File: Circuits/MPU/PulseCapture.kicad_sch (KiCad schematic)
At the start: 24 parts, among them U26 LT1715, U27 ADA4805-2ARMZ, U31 AD7984BRMZ

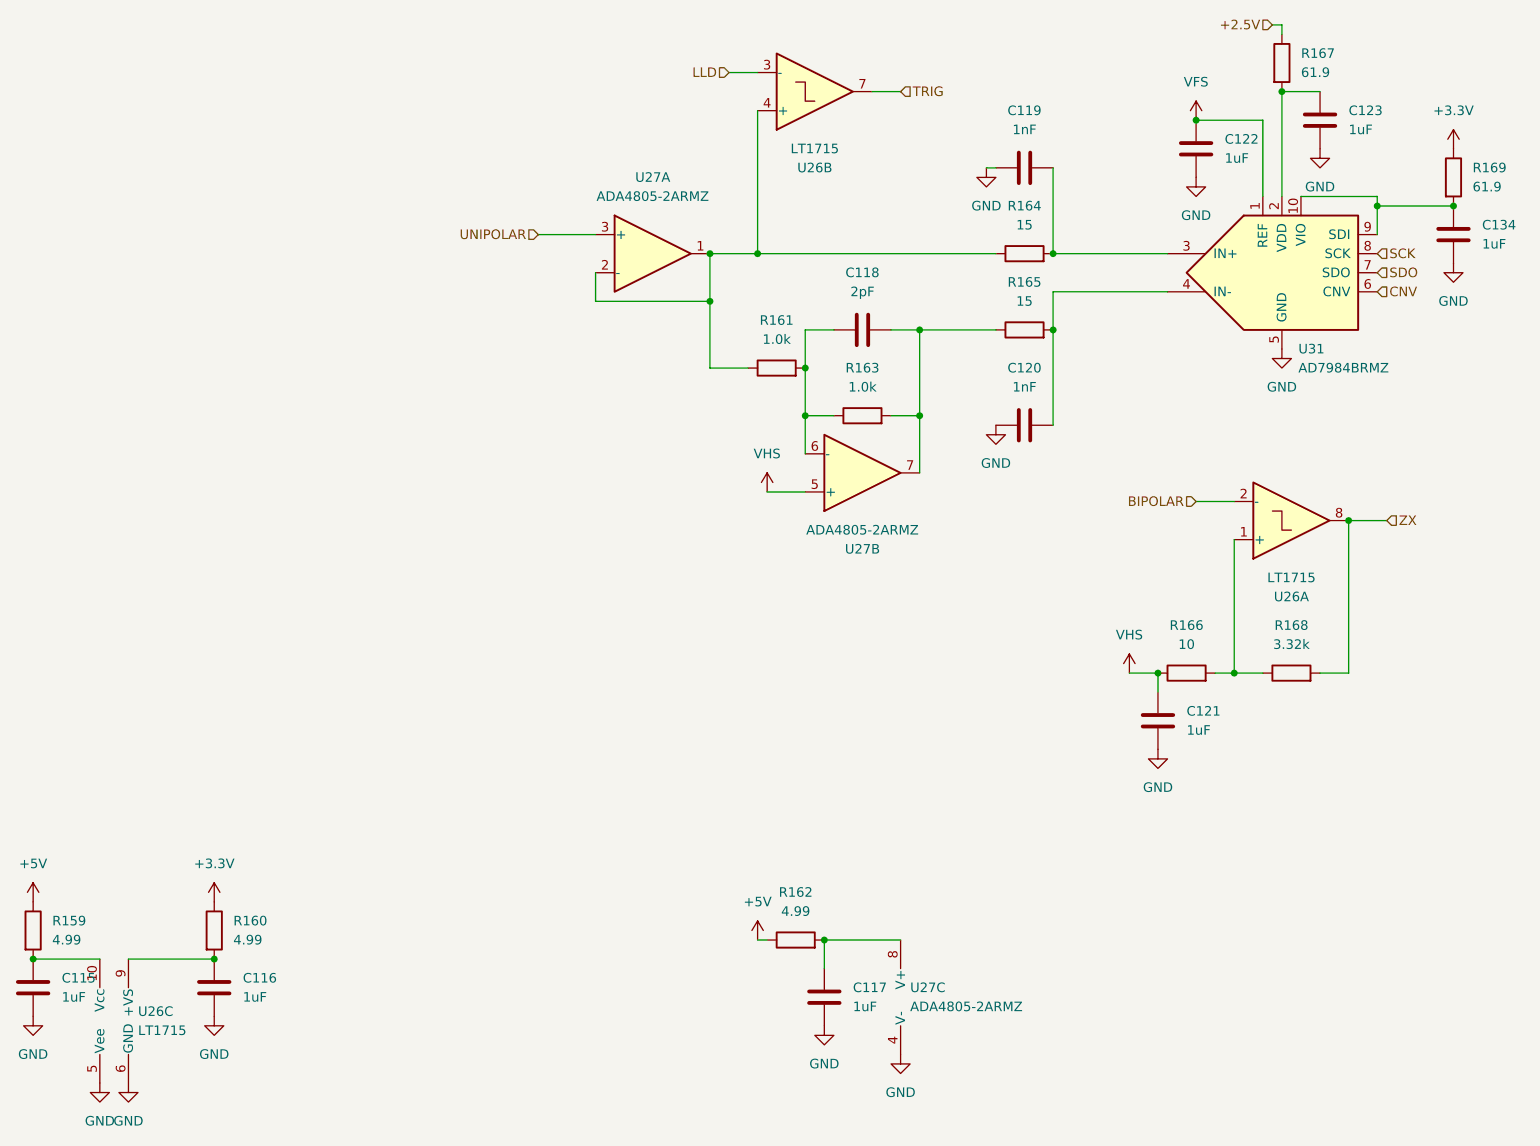
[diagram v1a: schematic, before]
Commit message: PPS is RS422, add MXINH
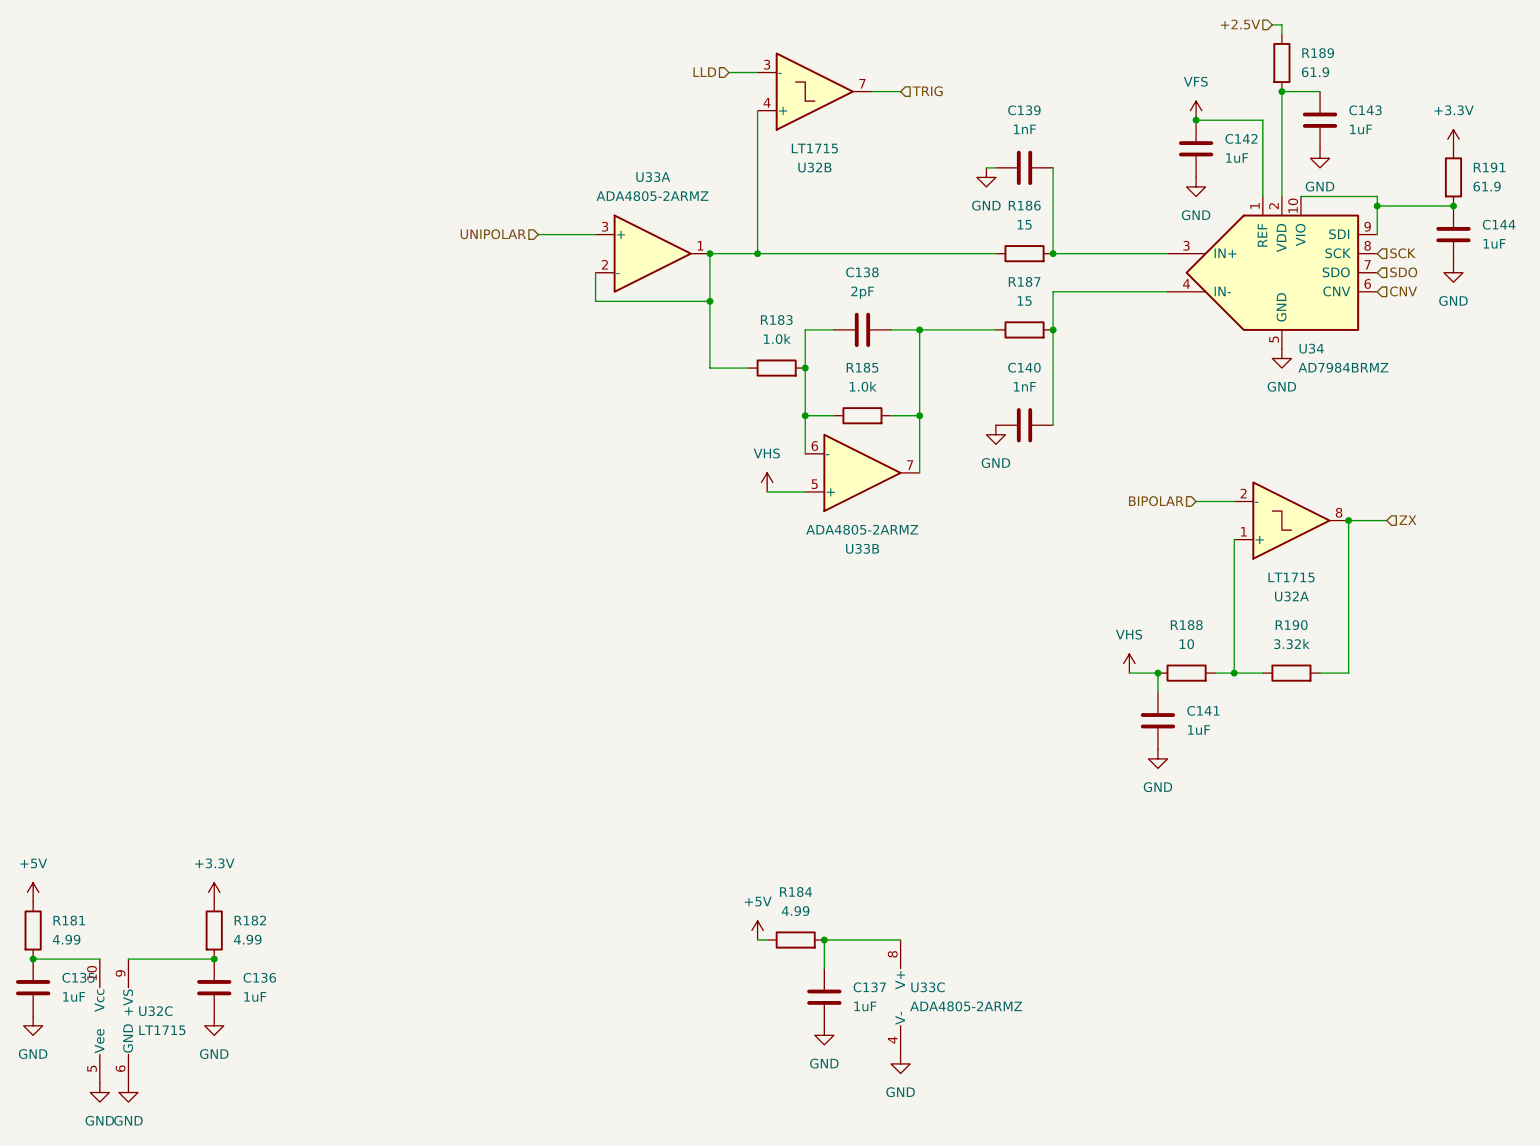
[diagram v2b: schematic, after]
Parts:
- renumbered C115 to C135, C116 to C136, C117 to C137, C118 to C138, C119 to C139, C120 to C140, C121 to C141, C122 to C142, C123 to C143, C134 to C144, R159 to R181, R160 to R182, R161 to R183, R162 to R184, R163 to R185, R164 to R186, R165 to R187, R166 to R188, R167 to R189, R168 to R190, R169 to R191, U26 to U32, U27 to U33, U31 to U34
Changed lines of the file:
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@@
 	(title_block
 		(title "QuERI MPU")
-		(date "2024-06-05")
-		(rev "RR1")
+		(date "2024-06-27")
+		(rev "RR3")
 		(company "Noqsi Aerospace Ltd")
 		(comment 1 "15 Blanchard Avenue, Billerica MA 01821")
@@
 		(dnp no)
 		(fields_autoplaced yes)
-		(property "Reference" "#PWR0230"
+		(property "Reference" "#PWR0270"
 			(at 31.75 201.93 0)
 			(effects
@@
 		(dnp no)
 		(fields_autoplaced yes)
-		(property "Reference" "C123"
+		(property "Reference" "C143"
 			(at 198.12 66.04 0)
 			(effects
@@
 		(dnp no)
 		(fields_autoplaced yes)
-		(property "Reference" "C120"
+		(property "Reference" "C140"
 			(at 154.94 100.33 90)
 			(effects
@@
 		(on_board yes)
 		(dnp no)
-		(property "Reference" "U27"
+		(property "Reference" "U33"
 			(at 133.35 124.46 0)
 			(effects
@@
 		(dnp no)
 		(fields_autoplaced yes)
-		(property "Reference" "C117"
+		(property "Reference" "C137"
 			(at 132.08 182.88 0)
 			(effects
@@
 		(dnp no)
 		(fields_autoplaced yes)
-		(property "Reference" "C134"
+		(property "Reference" "C144"
 			(at 215.9 81.28 0)
 			(effects
@@
 		(dnp no)
 		(fields_autoplaced yes)
-		(property "Reference" "R165"
+		(property "Reference" "R187"
 			(at 154.94 88.9 90)
 			(effects
@@
 		(dnp no)
 		(fields_autoplaced yes)
-		(property "Reference" "#PWR0241"
+		(property "Reference" "#PWR0281"
 			(at 172.72 157.48 0)
 			(effects
@@
 		(dnp no)
 		(fields_autoplaced yes)
-		(property "Reference" "#PWR0229"
+		(property "Reference" "#PWR0269"
 			(at 22.86 193.04 0)
 			(effects
@@
 		(dnp no)
 		(fields_autoplaced yes)
-		(property "Reference" "U27"
+		(property "Reference" "U33"
 			(at 139.7 182.88 0)
 			(effects
@@
 		(dnp no)
 		(fields_autoplaced yes)
-		(property "Reference" "C118"
+		(property "Reference" "C138"
 			(at 133.35 87.63 90)
 			(effects
@@
 		(dnp no)
 		(fields_autoplaced yes)
-		(property "Reference" "#PWR0232"
+		(property "Reference" "#PWR0272"
 			(at 46.99 175.26 0)
 			(effects
@@
 		(dnp no)
 		(fields_autoplaced yes)
-		(property "Reference" "#PWR0267"
+		(property "Reference" "#PWR0287"
 			(at 212.09 92.71 0)
 			(effects
@@
 		(dnp no)
 		(fields_autoplaced yes)
-		(property "Reference" "U27"
+		(property "Reference" "U33"
 			(at 105.41 74.93 0)
 			(effects
@@
 		(dnp no)
 		(fields_autoplaced yes)
-		(property "Reference" "R162"
+		(property "Reference" "R184"
 			(at 124.46 170.18 90)
 			(effects
@@
 		(dnp no)
 		(fields_autoplaced yes)
-		(property "Reference" "#PWR0228"
+		(property "Reference" "#PWR0268"
 			(at 22.86 175.26 0)
 			(effects
@@
 		(dnp no)
 		(fields_autoplaced yes)
-		(property "Reference" "R164"
+		(property "Reference" "R186"
 			(at 154.94 78.74 90)
 			(effects
@@
 		(dnp no)
 		(fields_autoplaced yes)
-		(property "Reference" "#PWR0243"
+		(property "Reference" "#PWR0283"
 			(at 177.8 81.28 0)
 			(effects
@@
 		(dnp no)
 		(fields_autoplaced yes)
-		(property "Reference" "#PWR0239"
+		(property "Reference" "#PWR0279"
 			(at 151.13 114.3 0)
 			(effects
@@
 		(dnp no)
 		(fields_autoplaced yes)
-		(property "Reference" "#PWR0246"
+		(property "Reference" "#PWR0286"
 			(at 212.09 74.93 0)
 			(effects
@@
 		(dnp no)
 		(fields_autoplaced yes)
-		(property "Reference" "#PWR0238"
+		(property "Reference" "#PWR0278"
 			(at 149.86 80.01 0)
 			(effects
@@
 		(dnp no)
 		(fields_autoplaced yes)
-		(property "Reference" "R167"
+		(property "Reference" "R189"
 			(at 191.77 58.42 0)
 			(effects
@@
 		(dnp no)
 		(fields_autoplaced yes)
-		(property "Reference" "R166"
+		(property "Reference" "R188"
 			(at 176.53 134.62 90)
 			(effects
@@
 		(dnp no)
 		(fields_autoplaced yes)
-		(property "Reference" "#PWR0235"
+		(property "Reference" "#PWR0275"
 			(at 120.65 120.65 0)
 			(effects
@@
 		(dnp no)
 		(fields_autoplaced yes)
-		(property "Reference" "C116"
+		(property "Reference" "C136"
 			(at 50.8 181.61 0)
 			(effects
@@
 		(dnp no)
 		(fields_autoplaced yes)
-		(property "Reference" "C115"
+		(property "Reference" "C135"
 			(at 26.67 181.61 0)
 			(effects
@@
 		(on_board yes)
 		(dnp no)
-		(property "Reference" "U26"
+		(property "Reference" "U32"
 			(at 190.5 130.81 0)
 			(effects
@@
 		(dnp no)
 		(fields_autoplaced yes)
-		(property "Reference" "#PWR0236"
+		(property "Reference" "#PWR0276"
 			(at 128.27 194.31 0)
 			(effects
@@
 		(dnp no)
 		(fields_autoplaced yes)
-		(property "Reference" "C122"
+		(property "Reference" "C142"
 			(at 181.61 69.85 0)
 			(effects
@@
 		(dnp no)
 		(fields_autoplaced yes)
-		(property "Reference" "#PWR0245"
+		(property "Reference" "#PWR0285"
 			(at 194.31 77.47 0)
 			(effects
@@
 		(dnp no)
 		(fields_autoplaced yes)
-		(property "Reference" "C119"
+		(property "Reference" "C139"
 			(at 154.94 66.04 90)
 			(effects
@@
 		(dnp no)
 		(fields_autoplaced yes)
-		(property "Reference" "C121"
+		(property "Reference" "C141"
 			(at 176.53 146.05 0)
 			(effects
@@
 		(dnp no)
 		(fields_autoplaced yes)
-		(property "Reference" "R169"
+		(property "Reference" "R191"
 			(at 214.63 73.66 0)
 			(effects
@@
 		(dnp no)
 		(fields_autoplaced yes)
-		(property "Reference" "#PWR0242"
+		(property "Reference" "#PWR0282"
 			(at 177.8 71.12 0)
 			(effects
@@
 		(dnp no)
 		(fields_autoplaced yes)
-		(property "Reference" "R159"
+		(property "Reference" "R181"
 			(at 25.4 173.99 0)
 			(effects
@@
 		(dnp no)
 		(fields_autoplaced yes)
-		(property "Reference" "R161"
+		(property "Reference" "R183"
 			(at 121.92 93.98 90)
 			(effects
@@
 		(dnp no)
 		(fields_autoplaced yes)
-		(property "Reference" "R160"
+		(property "Reference" "R182"
 			(at 49.53 173.99 0)
 			(effects
@@
 		(dnp no)
 		(fields_autoplaced yes)
-		(property "Reference" "U31"
+		(property "Reference" "U34"
 			(at 191.4241 97.79 0)
 			(effects
@@
 		(dnp no)
 		(fields_autoplaced yes)
-		(property "Reference" "#PWR0237"
+		(property "Reference" "#PWR0277"
 			(at 138.43 198.12 0)
 			(effects
@@
 		(dnp no)
 		(fields_autoplaced yes)
-		(property "Reference" "R163"
+		(property "Reference" "R185"
 			(at 133.35 100.33 90)
 			(effects
@@
 		(dnp no)
 		(fields_autoplaced yes)
-		(property "Reference" "#PWR0233"
+		(property "Reference" "#PWR0273"
 			(at 46.99 193.04 0)
 			(effects
@@
 		(dnp no)
 		(fields_autoplaced yes)
-		(property "Reference" "#PWR0244"
+		(property "Reference" "#PWR0284"
 			(at 189.23 104.14 0)
 			(effects
@@
 		(dnp no)
 		(fields_autoplaced yes)
-		(property "Reference" "#PWR0240"
+		(property "Reference" "#PWR0280"
 			(at 168.91 144.78 0)
 			(effects
@@
 		(dnp no)
 		(fields_autoplaced yes)
-		(property "Reference" "#PWR0234"
+		(property "Reference" "#PWR0274"
 			(at 119.38 180.34 0)
 			(effects
@@
 		(on_board yes)
 		(dnp no)
-		(property "Reference" "U26"
+		(property "Reference" "U32"
 			(at 127 73.66 0)
 			(effects
@@
 		(dnp no)
 		(fields_autoplaced yes)
-		(property "Reference" "U26"
+		(property "Reference" "U32"
 			(at 36.83 186.055 0)
 			(effects
@@
 		(dnp no)
 		(fields_autoplaced yes)
-		(property "Reference" "R168"
+		(property "Reference" "R190"
 			(at 190.5 134.62 90)
 			(effects
@@
 		(dnp no)
 		(fields_autoplaced yes)
-		(property "Reference" "#PWR0231"
+		(property "Reference" "#PWR0271"
 			(at 35.56 201.93 0)
 			(effects
